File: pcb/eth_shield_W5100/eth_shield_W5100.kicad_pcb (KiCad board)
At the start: 2 copper layers, 36 x 59 mm, 46 parts, among them J1 Conn_02x05_Odd_Even, J2 HR911105A, U1 LM1117-3.3, U2 W5100, Y1 Crystal

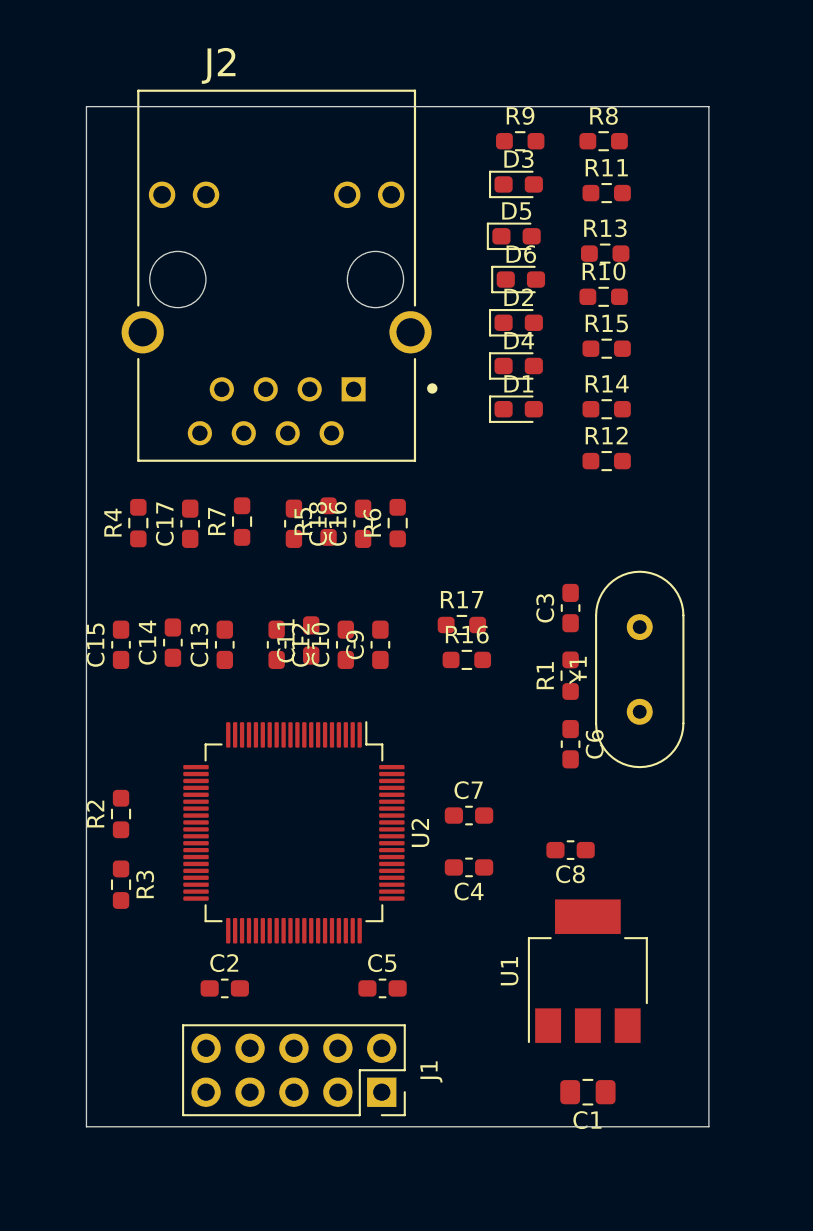
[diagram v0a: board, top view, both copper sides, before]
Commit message: Se termina el routeo, se agregan comentarios y detalles
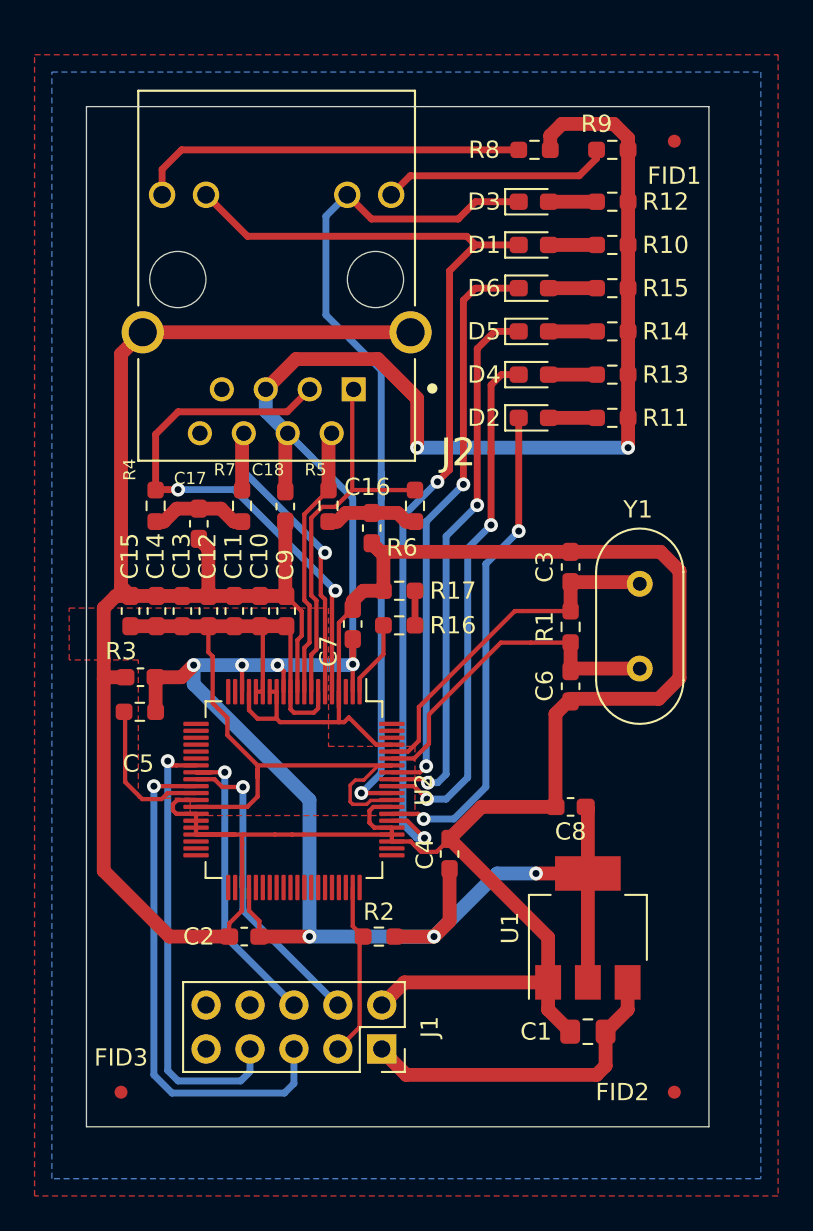
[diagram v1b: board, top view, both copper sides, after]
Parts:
- added FID1: Fiducial, Fiducial:Fiducial_0.75mm_Mask1.5mm, F.Cu at (139.0, 32.0)
- added FID2: Fiducial, Fiducial:Fiducial_0.75mm_Mask1.5mm, F.Cu at (139.0, 87.0)
- added FID3: Fiducial, Fiducial:Fiducial_0.75mm_Mask1.5mm, F.Cu at (107.0, 87.0)
- moved C5 22.8 mm to (108.1, 63.0), turned to 180 degrees
- moved R2 16.5 mm to (121.9, 78.0), turned to 0 degrees
- moved R12 15.0 mm to (135.4, 35.5), turned to 180 degrees
- moved R11 13.0 mm to (135.4, 48.0), turned to 180 degrees
- moved C7 13.0 mm to (120.4, 59.9), turned to 90 degrees
- moved R3 10.1 mm to (108.1, 65.0), turned to 0 degrees
- moved D1 9.54 mm to (130.9, 38.0)
- moved R13 7.01 mm to (135.4, 45.5), turned to 180 degrees
- moved C9 5.79 mm to (116.5, 59.2)
- moved D5 5.59 mm to (130.9, 43.0)
- moved D2 5.57 mm to (130.9, 48.0)
- moved R9 5.35 mm to (135.4, 32.5)
- moved C10 5.32 mm to (115.0, 59.2)
- moved C11 4.76 mm to (113.5, 59.2)
- moved R14 4.51 mm to (135.4, 43.0), turned to 180 degrees
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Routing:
- net GND: track 0.00 -> 211.5 mm
- net +3V3: track 0.00 -> 154.7 mm, vias 0 -> 9
- net /LINK_LEDn: track 0.00 -> 58.4 mm, vias 0 -> 2
- net /FDX_LEDn: track 0.00 -> 51.0 mm, vias 0 -> 1
- net +1V8: track 0.00 -> 50.4 mm
- net /RXp: track 0.00 -> 35.2 mm, vias 0 -> 2
- net /TX_LEDn: track 0.00 -> 33.5 mm, vias 0 -> 2
- net /RX_LEDn: track 0.00 -> 31.6 mm, vias 0 -> 2
- net /COL_LEDn: track 0.00 -> 30.3 mm, vias 0 -> 2
- net /SCK: track 0.00 -> 30.0 mm, vias 0 -> 1
- net /SPD_LEDn: track 0.00 -> 28.5 mm, vias 0 -> 2
- net /MISO: track 0.00 -> 26.2 mm, vias 0 -> 1
- net /RXn: track 0.00 -> 25.7 mm, vias 0 -> 1
- net /TXp: track 0.00 -> 22.8 mm
- net Net-(J2-Pad12): track 0.00 -> 22.6 mm
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- added copper zone on F.Cu, net +1V8
- added copper zone on B.Cu, net +3V3
- added copper zone on F.Cu, net GND
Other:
- net class Default: clearance 0.2 -> 0.15
- rule trace_clearance: 0.2 -> 0.15
- rule trace_min: 0.2 -> 0.15
- board text added: "Grillas: - 1.0 mm: Contorno del PCB - 0.5 mm: Componentes - 0.1 mm: Routeo"
- board text added: "Notas: - Se usaron pistas y clearence adorde a los pads del W5100 - Se usaron componentes 0603, porque son los standar en mi empresa. - Los componentes 0603 son handsoldering."
- board text added: "Reglas: - 0.15 mm: Clearence - 0.25 mm: Pistas - 0.80 mm: Pad de via - 0.40 mm: Agujero de via"
- board text added: "Stack Up: - Top: F.cu - Bottom: B.cu"

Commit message: Se agrega agujeros y se hacen las correciones indicadas por el docente
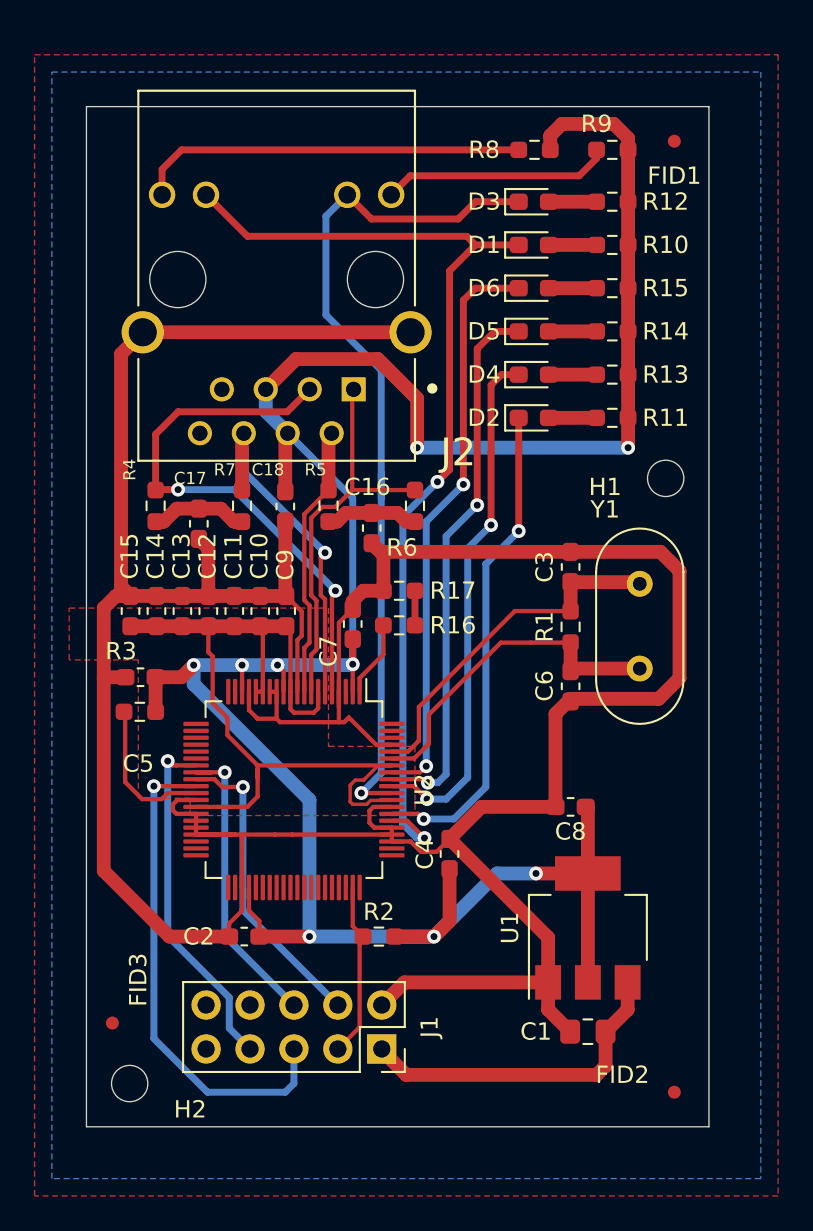
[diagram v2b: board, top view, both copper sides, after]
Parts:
- added H1: MountingHole, MountingHole:MountingHole_2.1mm, F.Cu at (138.5, 51.5)
- added H2: MountingHole, MountingHole:MountingHole_2.1mm, F.Cu at (107.5, 86.5)
- moved FID3 4.03 mm to (106.5, 83.0)
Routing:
- net /MISO: track 26.2 -> 20.4 mm
- net /SCK: track 30.0 -> 28.7 mm

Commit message: Se agregan las correciones que se hicieron para la presentación
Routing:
- net /MISO: track 20.4 -> 22.1 mm
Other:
- board text added: "CESE - FIUBA Rev 0"
- board text added: "Ind. Arg."
- board text added: "Notas: - Se usaron pistas y clearence adorde a los pads del W5100 - Se usaron componentes 0603, porque son los standar en mi empresa. - Los componentes 0603 son handsoldering. - La terminación utilizada será HASL Lead Free"
- board text removed: "Notas: - Se usaron pistas y clearence adorde a los pads del W5100 - Se usaron componentes 0603, porque son los standar en mi empresa. - Los componentes 0603 son handsoldering."
